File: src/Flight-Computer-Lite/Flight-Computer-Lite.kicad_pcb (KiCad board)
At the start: 4 copper layers, 74 parts, among them J1 Jumper_NO, J2 Jumper_NO, P1 1546551-2, P2 3220-20-0200-00, P3 USB, P4 1984659, Q1 QS5U17TR, Q2 QS5U17TR, U1 STM32H750VBTx, U2 LMS8117AMP-3.3_NOPB, U3 SST25VF040B-50-4I-S2AE-T, U4 CP2102-GMR(QFN28), U5 TS391IYLT, U6 BMP390, U7 TS391IYLT, U8 TS391IYLT, Y1 ECS-240-18-33-JGN-TR

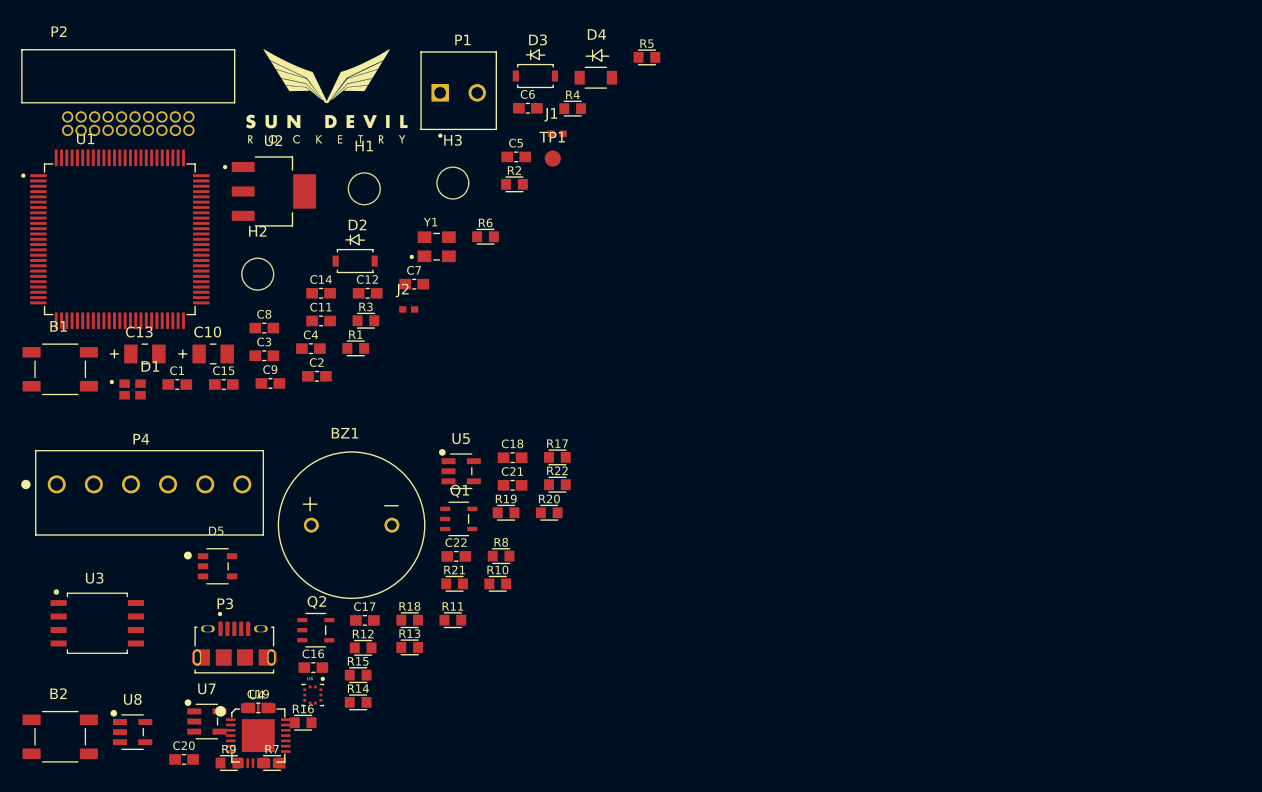
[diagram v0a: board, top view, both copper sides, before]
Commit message: finalized board outline and component placements
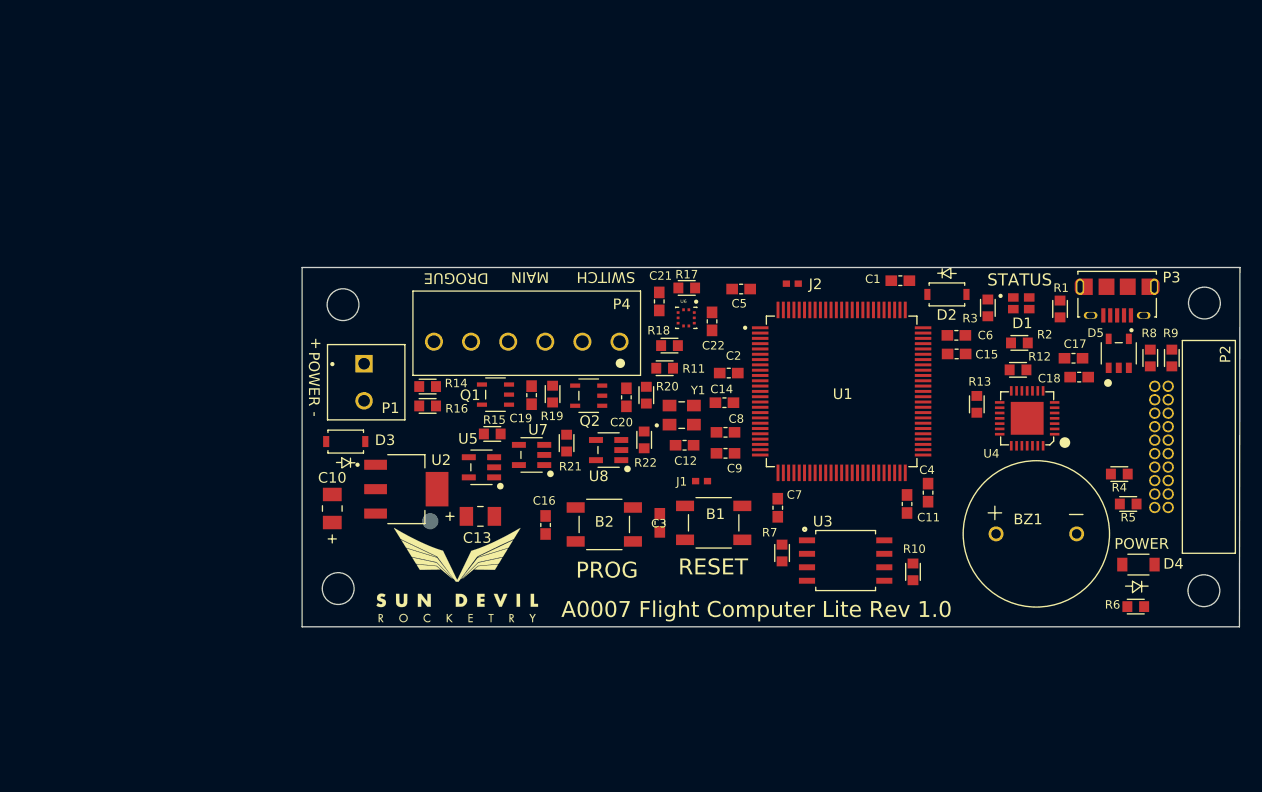
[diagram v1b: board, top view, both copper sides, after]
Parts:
- added H4: Mounting-Hole, Flight-Computer-Lite:MountingHole_3mm, F.Cu at (154.2, 106.8)
- TP1: moved to B.Cu
- moved P2 102.9 mm to (232.5, 93.4), turned to -90 degrees
- moved R9 96.8 mm to (232.8, 85.0), turned to -90 degrees
- moved P3 90.3 mm to (227.7, 78.3), turned to 180 degrees
- moved H2 89.3 mm to (235.9, 79.9)
- moved H1 87.8 mm to (235.9, 107.0)
- moved D5 87.3 mm to (227.8, 84.6), turned to 90 degrees
- moved D1 84.2 mm to (218.6, 79.9)
- moved U4 78.4 mm to (219.2, 90.7), turned to 180 degrees
- moved C17 71.3 mm to (223.6, 85.1)
- moved U3 70.8 mm to (202.1, 104.1)
- moved R6 70.5 mm to (229.4, 108.5)
- moved U1 69.6 mm to (201.7, 88.2)
- moved C15 69.2 mm to (212.5, 84.7)
- moved C1 68.9 mm to (207.2, 77.7)
- moved D4 68.7 mm to (229.7, 104.5), turned to 180 degrees
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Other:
- board outline added: 88.4 x 33.9 mm
- board text added: "+"
- board text added: "-"
- board text added: "A0007 Flight Computer Lite Rev 1.0"
- board text added: "DROGUE"
- board text added: "MAIN"
- board text added: "POWER"
- board text added: "PROG"
- board text added: "RESET"
- board text added: "STATUS"
- board text added: "SWITCH"

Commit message: finalized rev1 routing
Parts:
- moved D2 9.67 mm to (221.2, 80.6), turned to -90 degrees
- moved C16 8.92 mm to (182.7, 100.9), turned to -90 degrees
- moved C3 8.44 mm to (193.0, 100.3), turned to -90 degrees
- moved J1 8.32 mm to (192.9, 103.7), turned to 90 degrees
- moved R3 4.94 mm to (210.6, 79.4)
- moved R1 4.73 mm to (217.6, 79.9)
- moved R4 4.64 mm to (229.4, 91.6), turned to 90 degrees
- moved R5 4.01 mm to (228.0, 94.9)
- moved R15 4.00 mm to (168.5, 96.2)
- moved D1 3.77 mm to (214.9, 79.7)
- moved R2 2.41 mm to (216.1, 83.0), turned to 90 degrees
- moved U5 2.23 mm to (167.6, 93.1)
- moved B2 2.19 mm to (177.1, 100.9), turned to 180 degrees
- moved R11 2.14 mm to (183.9, 84.2), turned to 90 degrees
- moved R20 2.06 mm to (184.6, 86.9), turned to 180 degrees
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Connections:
- U1 pad 25: unconnected-(U1-Pad25) -> PROG
- U1 pad 45: PROG -> unconnected-(U1-Pad45)
- U1 pad 5: unconnected-(U1-Pad5) -> MAIN
- U1 pad 59: ~{FLASH_WP} -> ~{FLASH_HOLD}
- U1 pad 60: ~{FLASH_HOLD} -> ~{FLASH_WP}
- U1 pad 87: MAIN -> unconnected-(U1-Pad87)
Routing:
- net Earth: track 0.00 -> 161.8 mm, vias 0 -> 26
- net VIN: track 0.00 -> 112.8 mm, vias 0 -> 1
- net 3.3V: track 0.00 -> 81.9 mm, vias 0 -> 19
- net NRST: track 0.00 -> 55.1 mm, vias 0 -> 1
- net ~{SWITCH}: track 0.00 -> 45.9 mm, vias 0 -> 2
- net VIN_SW: track 0.00 -> 44.5 mm
- net SWO: track 0.00 -> 37.2 mm, vias 0 -> 1
- net ~{FLASH_WP}: track 0.00 -> 35.5 mm
- net SWCLK: track 0.00 -> 34.9 mm, vias 0 -> 1
- net SWDIO: track 0.00 -> 32.2 mm, vias 0 -> 1
- net USB_DETECT: track 0.00 -> 30.7 mm, vias 0 -> 2
- net Net-(P4-Pad6): track 0.00 -> 30.2 mm, vias 0 -> 1
- net ~{MAIN_CONT}: track 0.00 -> 27.8 mm, vias 0 -> 2
- net DROGUE: track 0.00 -> 26.7 mm
- net VCOMP: track 0.00 -> 26.0 mm, vias 0 -> 3
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- added copper zone on In2.Cu, net 3.3V
- added copper zone on B.Cu, net Earth
- added copper zone on F.Cu, net Earth
- added copper zone on In1.Cu, net Earth

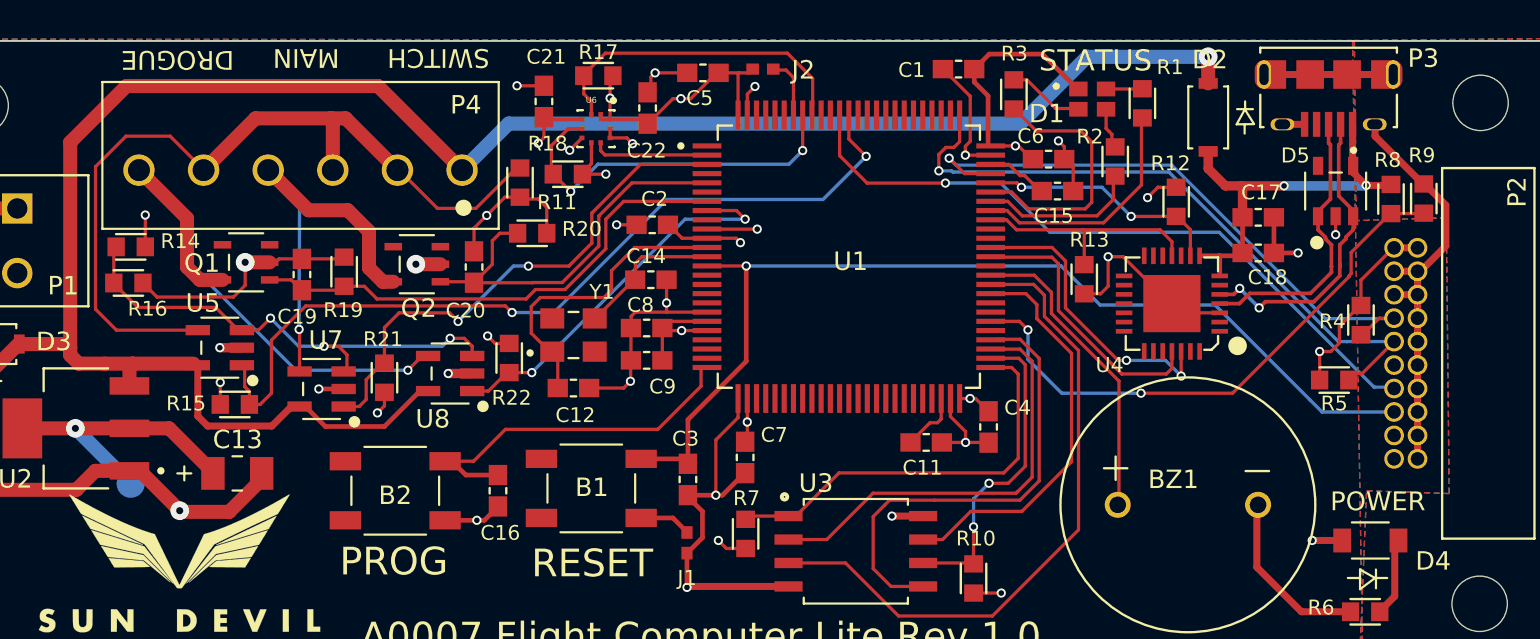
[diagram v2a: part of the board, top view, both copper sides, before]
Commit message: resolved DRC errors
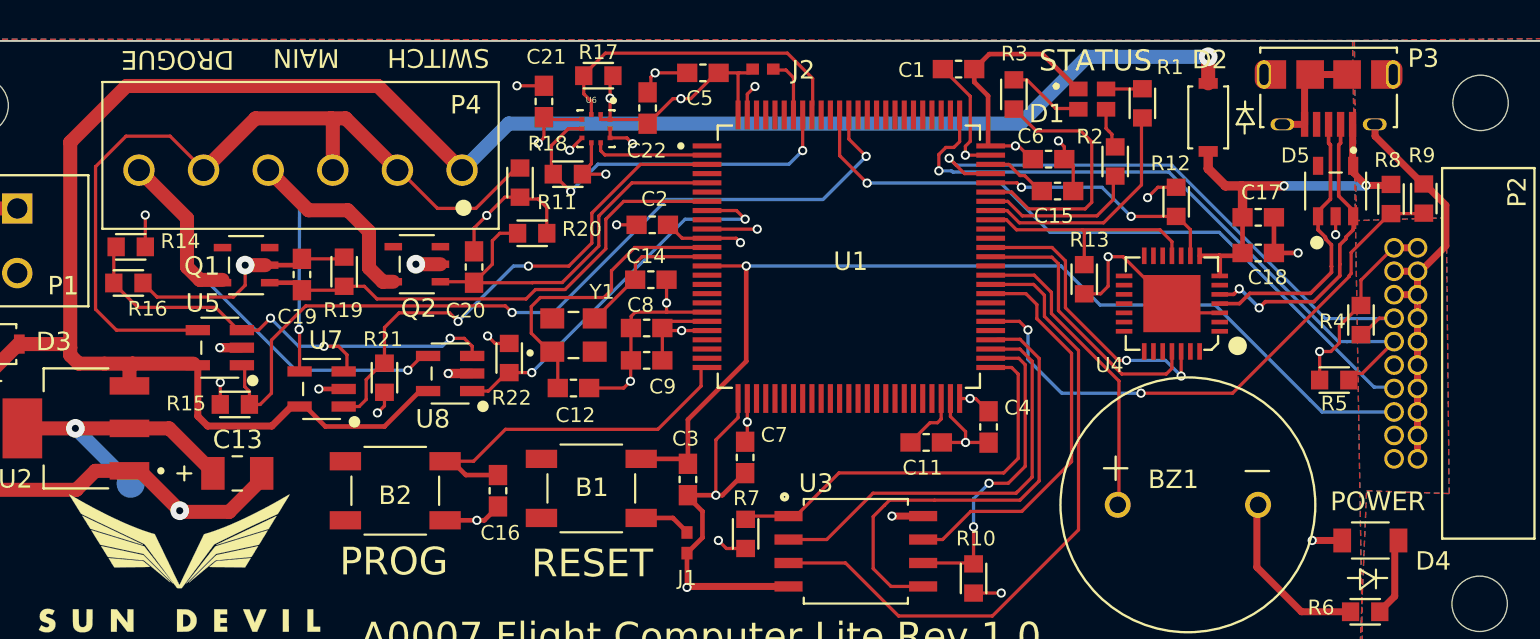
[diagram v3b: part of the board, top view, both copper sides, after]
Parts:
- moved Q1 0.15 mm to (169.1, 88.6)
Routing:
- net Earth: track 161.8 -> 159.0 mm

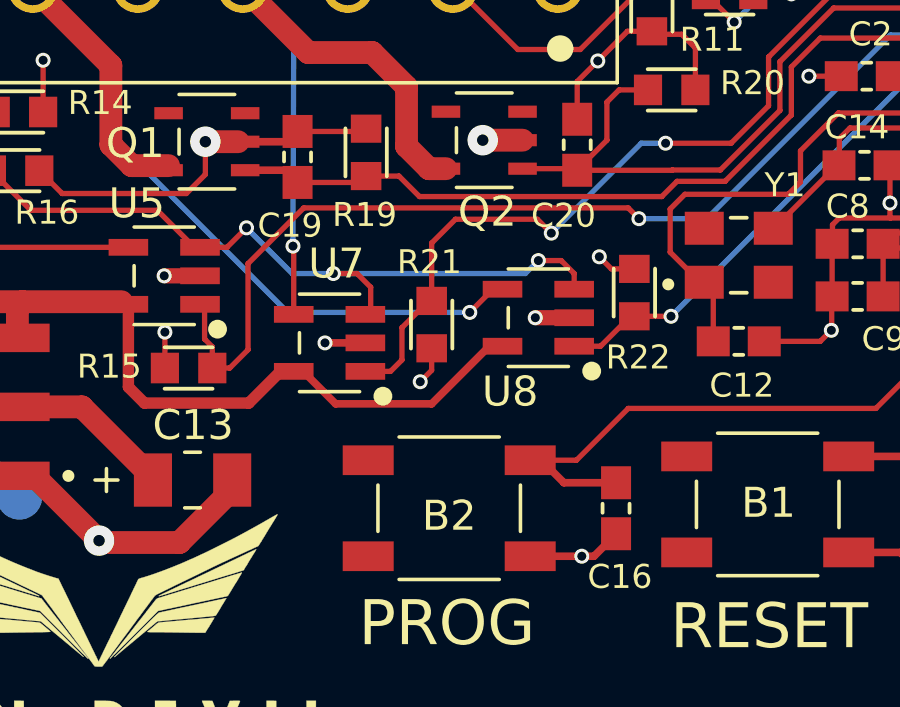
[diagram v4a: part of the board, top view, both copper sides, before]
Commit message: added ignition pull down resistors to layout
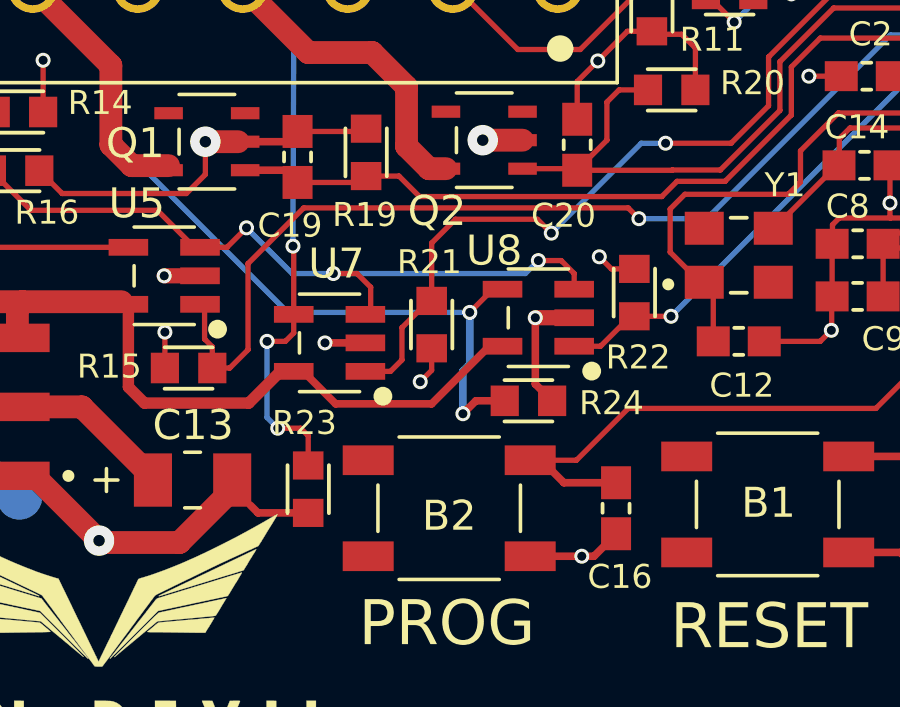
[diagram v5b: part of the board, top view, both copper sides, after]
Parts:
- added R23: 10k, Flight-Computer-Lite:RES_0603, F.Cu at (172.4, 100.2)
- added R24: 10k, Flight-Computer-Lite:RES_0603, F.Cu at (179.8, 97.3)
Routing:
- net Net-(P4-Pad4): track 21.9 -> 28.6 mm, vias 1 -> 3
- net Net-(P4-Pad6): track 30.2 -> 35.3 mm, vias 1 -> 2
- net Earth: track 159.0 -> 164.0 mm

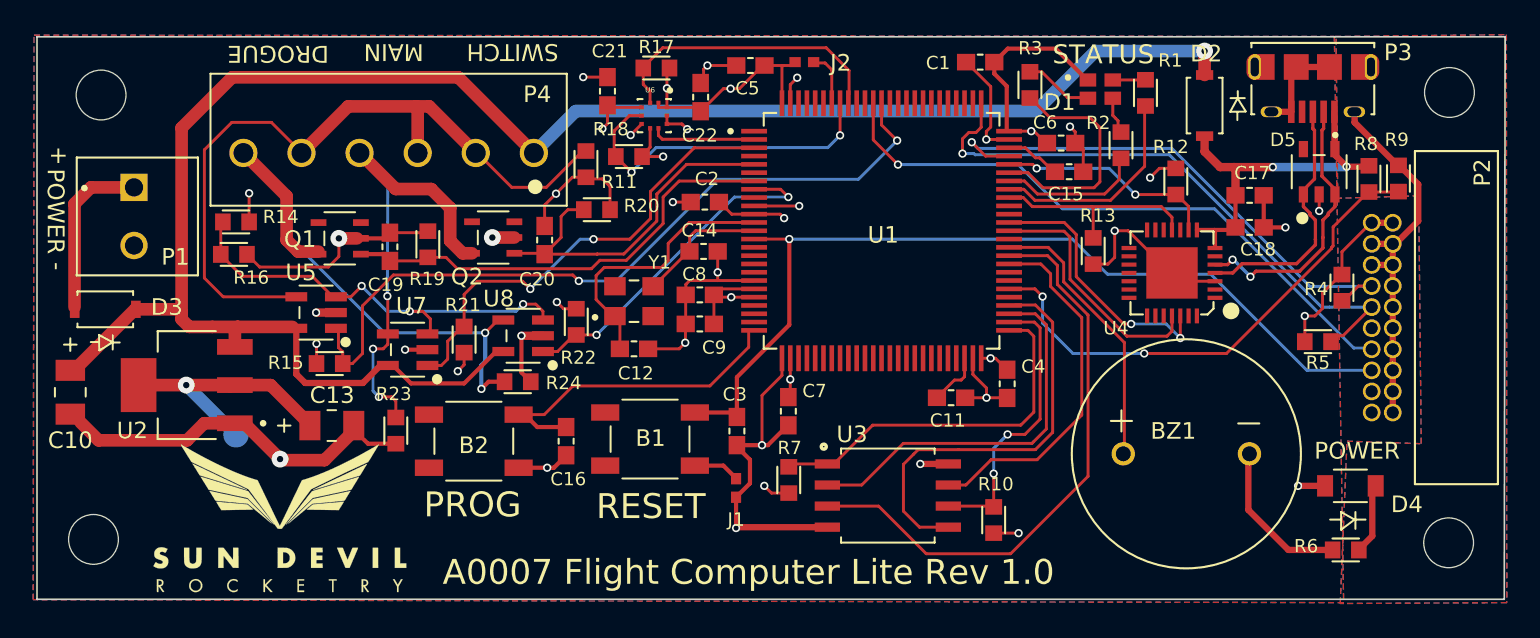
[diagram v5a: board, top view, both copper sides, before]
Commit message: reduced form factor
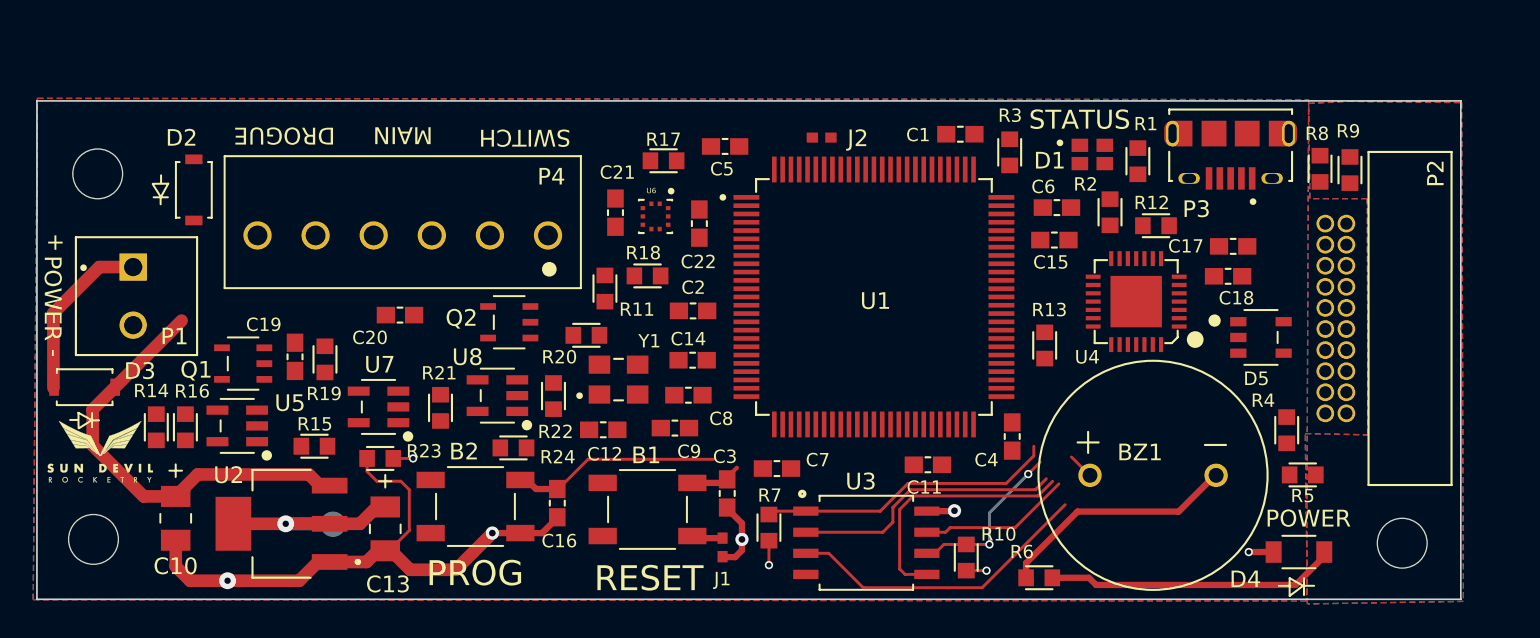
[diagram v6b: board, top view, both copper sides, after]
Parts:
- removed H2: Mounting-Hole, Flight-Computer-Lite:MountingHole_3mm
- B1: footprint Flight-Computer-Lite:PTS647SM38SMTR2LFS -> Flight-Computer:PTS647SM38SMTR2LFS
- LOGO1: footprint Flight-Computer-Lite:Logo -> Flight-Computer-Lite:logo_small
- moved D2 61.1 mm to (160.3, 85.7), turned to 90 degrees
- moved R6 18.5 mm to (211.2, 109.1)
- moved R14 13.3 mm to (158.0, 100.0), turned to -90 degrees
- moved LOGO1 11.5 mm to (154.6, 101.4)
- moved R16 10.8 mm to (159.8, 100.0), turned to -90 degrees
- moved D5 10.6 mm to (224.6, 94.6), turned to 0 degrees
- moved U2 10.1 mm to (165.6, 105.8)
- moved C10 9.90 mm to (159.2, 105.5)
- moved C20 9.82 mm to (172.7, 93.3), turned to 180 degrees
- moved Q1 9.53 mm to (163.2, 96.2)
- moved R19 9.30 mm to (168.2, 95.9)
- moved R4 9.21 mm to (226.1, 100.2)
- moved C19 8.75 mm to (166.4, 95.8)
- moved U5 8.32 mm to (162.9, 99.9)
- moved R5 8.08 mm to (227.1, 102.9)
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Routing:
- net Earth: track 164.0 -> 53.0 mm, vias 26 -> 4
- net VIN: track 112.8 -> 25.2 mm, vias 1 -> 0
- net 3.3V: track 81.6 -> 16.1 mm, vias 19 -> 4
- net NRST: track 55.1 -> 2.54 mm, vias 1 -> 0
- net ~{SWITCH}: track 45.8 -> 0.00 mm, vias 2 -> 0
- net VIN_SW: track 44.5 -> 0.00 mm
- net SWO: track 37.2 -> 0.00 mm, vias 1 -> 0
- net Net-(P4-Pad6): track 35.3 -> 0.00 mm, vias 2 -> 0
- net SWCLK: track 34.9 -> 0.00 mm, vias 1 -> 0
- net SWDIO: track 32.2 -> 0.00 mm, vias 1 -> 0
- net USB_DETECT: track 30.7 -> 0.00 mm, vias 2 -> 0
- net ~{MAIN_CONT}: track 27.7 -> 0.00 mm, vias 2 -> 0
- net Net-(P4-Pad4): track 28.6 -> 1.48 mm, vias 3 -> 1
- net DROGUE: track 26.5 -> 0.00 mm
- net VCOMP: track 25.9 -> 0.00 mm, vias 3 -> 0
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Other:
- board size 88.4 x 33.9 mm -> 85.8 x 30 mm
